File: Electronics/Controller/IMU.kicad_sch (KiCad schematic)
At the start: 9 parts, among them J10 CAN BUS, J9 TERM, U5 TJA1462ATK-0Z, U6 PESD2CANFD24V-TR

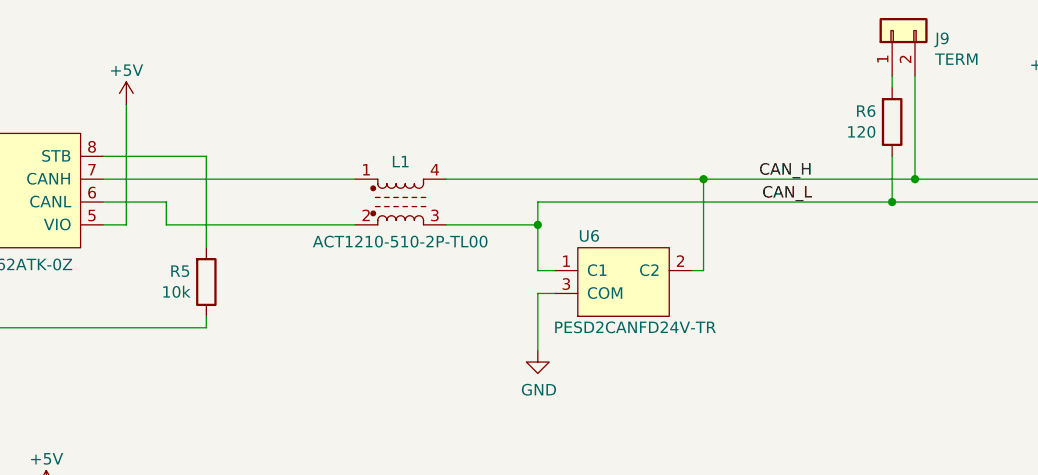
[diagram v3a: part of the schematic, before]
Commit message: Changed switches and lamps. Removed status LEDs. Working on PCB layout.
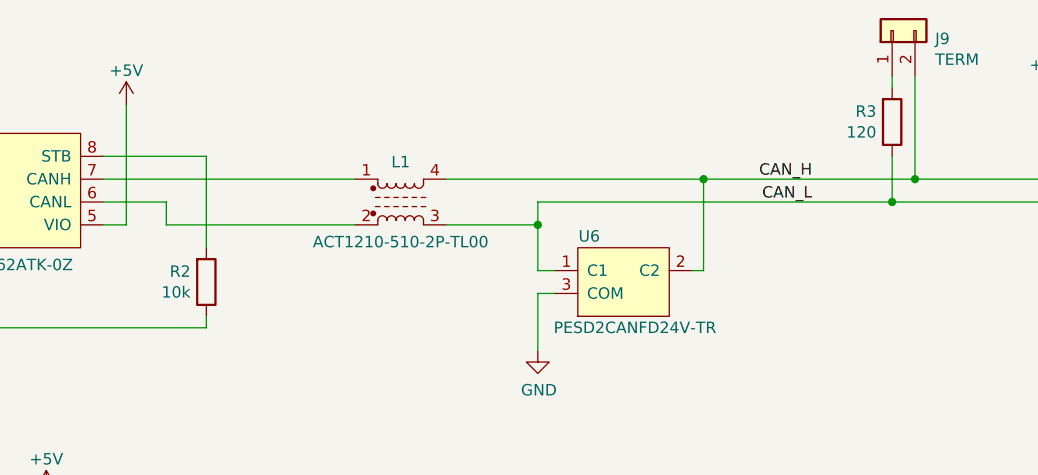
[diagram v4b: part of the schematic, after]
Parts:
- renumbered R5 to R2, R6 to R3
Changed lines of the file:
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@@
   (title_block
     (title "Tandem Leveller Controller")
-    (date "2025-02-16")
+    (date "2025-02-18")
     (rev "V1.0")
     (company "(C) andy@britishideas.com 2025")
@@
   (symbol (lib_id "power:GND") (at 215.265 92.71 0) (unit 1)
     (in_bom yes) (on_board yes) (dnp no)
-    (property "Reference" "#PWR026" (at 215.265 99.06 0)
+    (property "Reference" "#PWR023" (at 215.265 99.06 0)
       (effects (font (size 1.27 1.27)) hide)
     )
@@
       (project "Tandem Leveller Controller"
         (path "/56ffd1a6-bbed-43b6-8aa8-f23f49f76448/acdcb949-8386-481e-9890-88fc97609208"
-          (reference "#PWR026") (unit 1)
+          (reference "#PWR023") (unit 1)
         )
       )
@@
   (symbol (lib_id "power:+5V") (at 96.52 119.38 0) (unit 1)
     (in_bom yes) (on_board yes) (dnp no)
-    (property "Reference" "#PWR021" (at 96.52 123.19 0)
+    (property "Reference" "#PWR018" (at 96.52 123.19 0)
       (effects (font (size 1.27 1.27)) hide)
     )
@@
       (project "Tandem Leveller Controller"
         (path "/56ffd1a6-bbed-43b6-8aa8-f23f49f76448/acdcb949-8386-481e-9890-88fc97609208"
-          (reference "#PWR021") (unit 1)
+          (reference "#PWR018") (unit 1)
         )
       )
@@
   (symbol (lib_id "power:+5V") (at 85.725 119.38 0) (unit 1)
     (in_bom yes) (on_board yes) (dnp no)
-    (property "Reference" "#PWR019" (at 85.725 123.19 0)
+    (property "Reference" "#PWR016" (at 85.725 123.19 0)
       (effects (font (size 1.27 1.27)) hide)
     )
@@
       (project "Tandem Leveller Controller"
         (path "/56ffd1a6-bbed-43b6-8aa8-f23f49f76448/acdcb949-8386-481e-9890-88fc97609208"
-          (reference "#PWR019") (unit 1)
+          (reference "#PWR016") (unit 1)
         )
       )
@@
   (symbol (lib_id "Device:R") (at 190.5 78.105 0) (mirror x) (unit 1)
     (in_bom yes) (on_board yes) (dnp no)
-    (property "Reference" "R6" (at 188.7474 76.9366 0)
+    (property "Reference" "R3" (at 188.7474 76.9366 0)
       (effects (font (size 1.27 1.27)) (justify right))
     )
@@
       (project "Tandem Leveller Controller"
         (path "/56ffd1a6-bbed-43b6-8aa8-f23f49f76448/acdcb949-8386-481e-9890-88fc97609208"
-          (reference "R6") (unit 1)
+          (reference "R3") (unit 1)
         )
       )
@@
   (symbol (lib_id "power:GND") (at 79.375 102.235 0) (unit 1)
     (in_bom yes) (on_board yes) (dnp no)
-    (property "Reference" "#PWR018" (at 79.375 108.585 0)
+    (property "Reference" "#PWR015" (at 79.375 108.585 0)
       (effects (font (size 1.27 1.27)) hide)
     )
@@
       (project "Tandem Leveller Controller"
         (path "/56ffd1a6-bbed-43b6-8aa8-f23f49f76448/acdcb949-8386-481e-9890-88fc97609208"
-          (reference "#PWR018") (unit 1)
+          (reference "#PWR015") (unit 1)
         )
       )
@@
   (symbol (lib_id "power:+5V") (at 207.645 75.565 0) (unit 1)
     (in_bom yes) (on_board yes) (dnp no)
-    (property "Reference" "#PWR024" (at 207.645 79.375 0)
+    (property "Reference" "#PWR021" (at 207.645 79.375 0)
       (effects (font (size 1.27 1.27)) hide)
     )
@@
       (project "Tandem Leveller Controller"
         (path "/56ffd1a6-bbed-43b6-8aa8-f23f49f76448/acdcb949-8386-481e-9890-88fc97609208"
-          (reference "#PWR024") (unit 1)
+          (reference "#PWR021") (unit 1)
         )
       )
@@
   (symbol (lib_id "power:+5V") (at 105.41 76.2 0) (unit 1)
     (in_bom yes) (on_board yes) (dnp no)
-    (property "Reference" "#PWR022" (at 105.41 80.01 0)
+    (property "Reference" "#PWR019" (at 105.41 80.01 0)
       (effects (font (size 1.27 1.27)) hide)
     )
@@
       (project "Tandem Leveller Controller"
         (path "/56ffd1a6-bbed-43b6-8aa8-f23f49f76448/acdcb949-8386-481e-9890-88fc97609208"
-          (reference "#PWR022") (unit 1)
+          (reference "#PWR019") (unit 1)
         )
       )
@@
   (symbol (lib_id "power:GND") (at 151.13 103.505 0) (unit 1)
     (in_bom yes) (on_board yes) (dnp no)
-    (property "Reference" "#PWR023" (at 151.13 109.855 0)
+    (property "Reference" "#PWR020" (at 151.13 109.855 0)
       (effects (font (size 1.27 1.27)) hide)
     )
@@
       (project "Tandem Leveller Controller"
         (path "/56ffd1a6-bbed-43b6-8aa8-f23f49f76448/acdcb949-8386-481e-9890-88fc97609208"
-          (reference "#PWR023") (unit 1)
+          (reference "#PWR020") (unit 1)
         )
       )
@@
   (symbol (lib_id "Device:R") (at 114.3 95.885 0) (mirror x) (unit 1)
     (in_bom yes) (on_board yes) (dnp no)
-    (property "Reference" "R5" (at 112.5474 94.7166 0)
+    (property "Reference" "R2" (at 112.5474 94.7166 0)
       (effects (font (size 1.27 1.27)) (justify right))
     )
@@
       (project "Tandem Leveller Controller"
         (path "/56ffd1a6-bbed-43b6-8aa8-f23f49f76448/acdcb949-8386-481e-9890-88fc97609208"
-          (reference "R5") (unit 1)
+          (reference "R2") (unit 1)
         )
       )
@@
   (symbol (lib_id "power:+5V") (at 78.105 76.2 0) (unit 1)
     (in_bom yes) (on_board yes) (dnp no)
-    (property "Reference" "#PWR017" (at 78.105 80.01 0)
+    (property "Reference" "#PWR014" (at 78.105 80.01 0)
       (effects (font (size 1.27 1.27)) hide)
     )
@@
       (project "Tandem Leveller Controller"
         (path "/56ffd1a6-bbed-43b6-8aa8-f23f49f76448/acdcb949-8386-481e-9890-88fc97609208"
+          (reference "#PWR014") (unit 1)
+        )
+      )
+    )
+  )
+  (symbol (lib_id "power:GND") (at 85.725 133.985 0) (unit 1)
+    (in_bom yes) (on_board yes) (dnp no)
+    (property "Reference" "#PWR017" (at 85.725 140.335 0)
+      (effects (font (size 1.27 1.27)) hide)
+    )
+    (property "Value" "GND" (at 85.852 138.3792 0)
+      (effects (font (size 1.27 1.27)))
+    )
+    (property "Footprint" "" (at 85.725 133.985 0)
+      (effects (font (size 1.27 1.27)) hide)
+    )
+    (property "Datasheet" "" (at 85.725 133.985 0)
+      (effects (font (size 1.27 1.27)) hide)
+    )
+    (pin "1")
+    (instances
+      (project "Tandem Leveller Controller"
+        (path "/56ffd1a6-bbed-43b6-8aa8-f23f49f76448/acdcb949-8386-481e-9890-88fc97609208"
           (reference "#PWR017") (unit 1)
         )
@@
     )
   )
-  (symbol (lib_id "power:GND") (at 85.725 133.985 0) (unit 1)
-    (in_bom yes) (on_board yes) (dnp no)
-    (property "Reference" "#PWR020" (at 85.725 140.335 0)
-      (effects (font (size 1.27 1.27)) hide)
-    )
-    (property "Value" "GND" (at 85.852 138.3792 0)
-      (effects (font (size 1.27 1.27)))
-    )
-    (property "Footprint" "" (at 85.725 133.985 0)
-      (effects (font (size 1.27 1.27)) hide)
-    )
-    (property "Datasheet" "" (at 85.725 133.985 0)
-      (effects (font (size 1.27 1.27)) hide)
-    )
-    (pin "1")
-    (instances
-      (project "Tandem Leveller Controller"
-        (path "/56ffd1a6-bbed-43b6-8aa8-f23f49f76448/acdcb949-8386-481e-9890-88fc97609208"
-          (reference "#PWR020") (unit 1)
-        )
-      )
-    )
-  )
   (symbol (lib_id "EmSA:PESD2CANFD24V-T") (at 155.575 99.695 0) (unit 1)
     (in_bom yes) (on_board yes) (dnp no)
@@
   (symbol (lib_id "power:+12V") (at 215.265 75.565 0) (unit 1)
     (in_bom yes) (on_board yes) (dnp no)
-    (property "Reference" "#PWR025" (at 215.265 79.375 0)
+    (property "Reference" "#PWR022" (at 215.265 79.375 0)
       (effects (font (size 1.27 1.27)) hide)
     )
@@
       (project "Tandem Leveller Controller"
         (path "/56ffd1a6-bbed-43b6-8aa8-f23f49f76448/acdcb949-8386-481e-9890-88fc97609208"
-          (reference "#PWR025") (unit 1)
-        )
-      )
+          (reference "#PWR022") (unit 1)
+        )
+      )

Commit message: Working on PCB layout.
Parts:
- added J23: CAN, EmSA:DB9_RA_MALE_LD09P13A4, symbol Connector:DB9_Male
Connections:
- net CAN_H: now also J23.7
- net CAN_L: now also J23.2
- net GND: now also J23.3, J23.6
- no-connect marks 0 -> 5
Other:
- moved on the sheet: C1, C2, J10, J9, L1, R2, R3, U5, U6

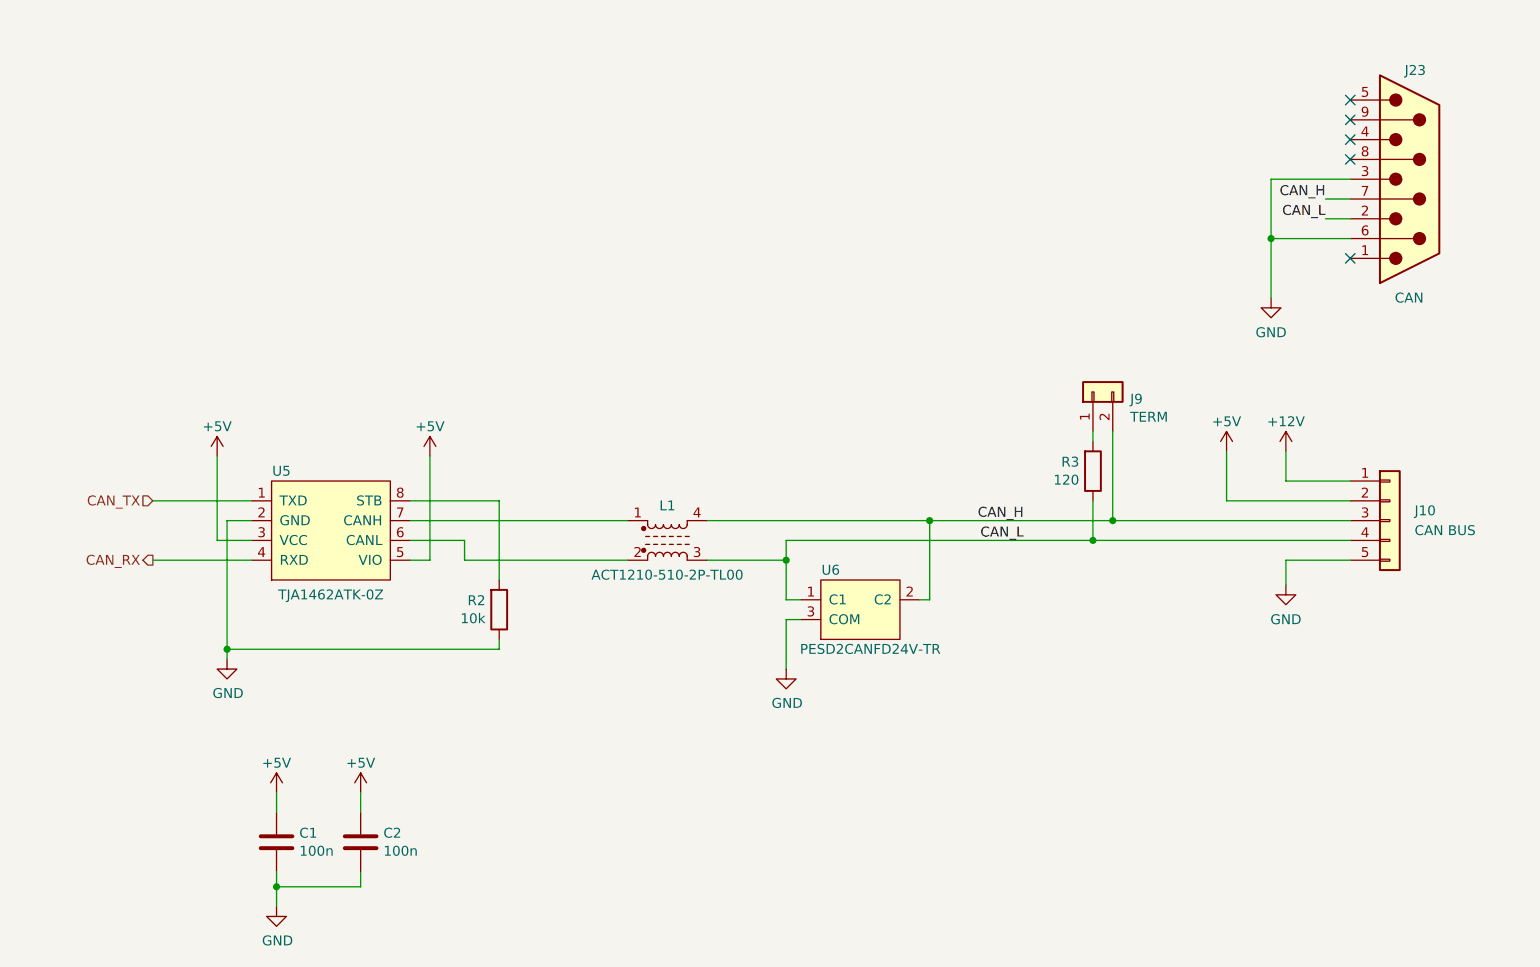
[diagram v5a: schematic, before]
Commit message: Moved controls from GPIO to CAN bus. Added two more CAN bus connectors. Changed GNSS SIM connector from pin header to JST-PH.
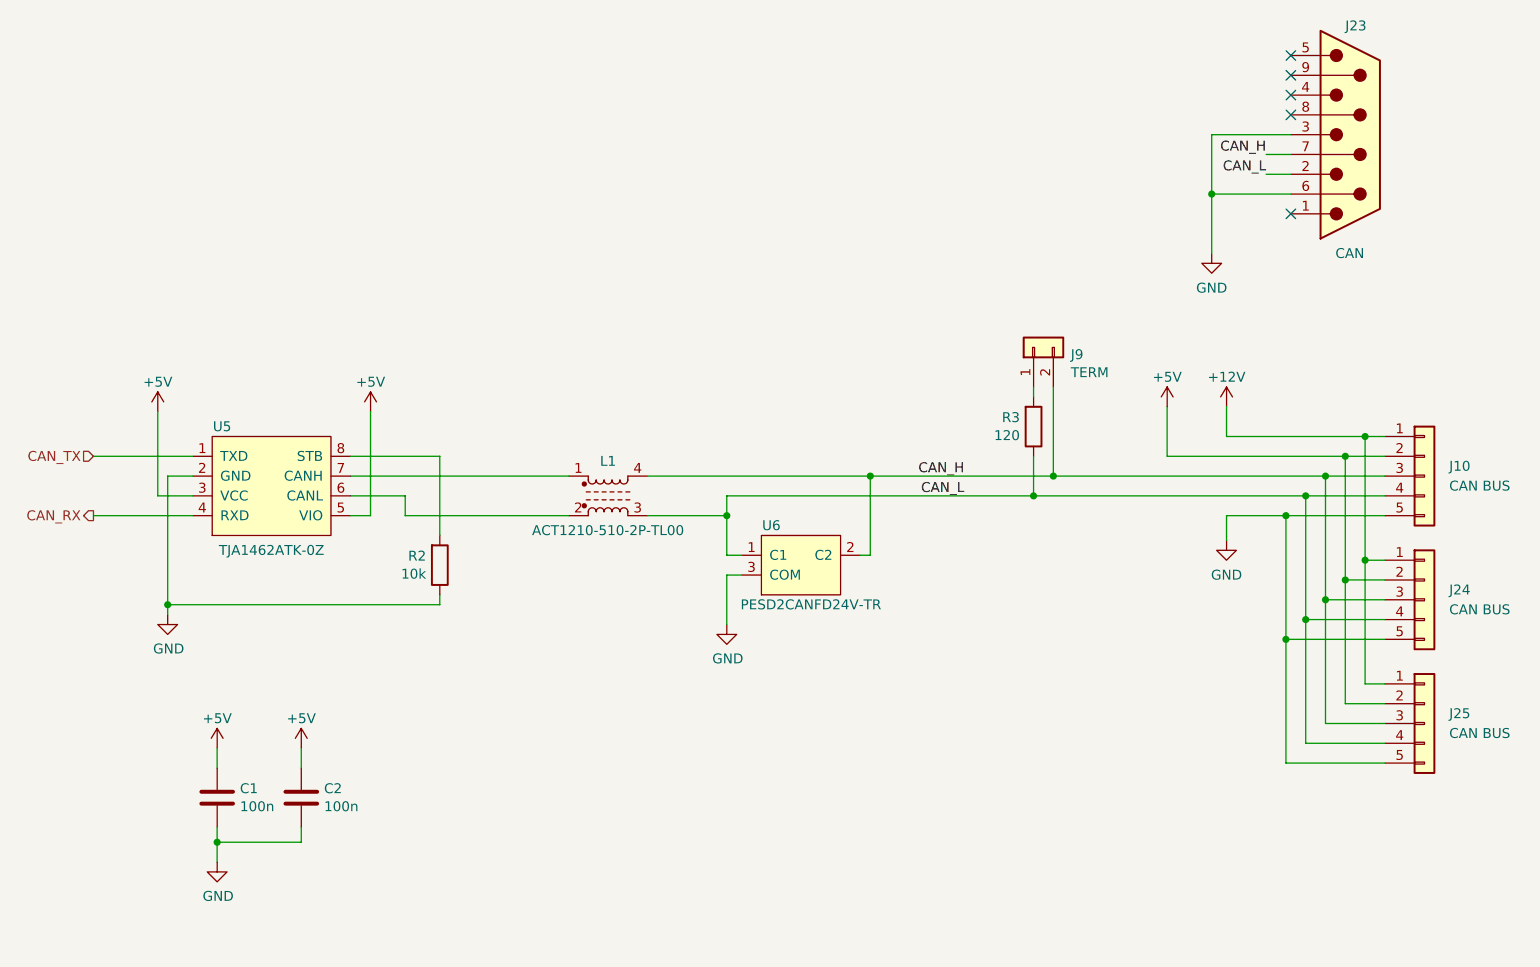
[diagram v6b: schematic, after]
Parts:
- added J24, J25: CAN BUS, Connector_JST:JST_PH_B5B-PH-K_1x05_P2.00mm_Vertical, symbol Connector_Generic:Conn_01x05
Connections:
- net +12V: now also J24.1 (Pin_1), J25.1 (Pin_1)
- net +5V: now also J24.2 (Pin_2), J25.2 (Pin_2)
- net CAN_H: now also J24.3 (Pin_3), J25.3 (Pin_3)
- net CAN_L: now also J24.4 (Pin_4), J25.4 (Pin_4)
- net GND: now also J24.5 (Pin_5), J25.5 (Pin_5)
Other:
- moved on the sheet: C1, C2, J10, J23, J9, L1, R2, R3, U5, U6

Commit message: Added 4.7uF caps to FT232RL on controller.
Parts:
- C1, C2: LCSC (none) -> C1711
- J10, J24, J25: LCSC (none) -> C157993
- J23: LCSC (none) -> C3103673
- J9: LCSC (none) -> C7494857
- L1: LCSC (none) -> C95572
- R2: LCSC (none) -> C17414
- R3: LCSC (none) -> C17437
- U5: LCSC (none) -> C3229259
- U6: LCSC (none) -> C552486
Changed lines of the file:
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@@
   (title_block
     (title "Tandem Leveller Controller")
-    (date "2025-02-22")
+    (date "2025-03-11")
     (rev "V1.0")
     (company "(C) andy@britishideas.com 2025")
@@
       (effects (font (size 1.27 1.27)) hide)
     )
+    (property "LCSC" "C157993" (at 229.235 96.52 0)
+      (effects (font (size 1.27 1.27)) hide)
+    )
     (pin "2")
     (pin "5")
@@
       (effects (font (size 1.27 1.27)) hide)
     )
+    (property "LCSC" "C157993" (at 229.235 112.395 0)
+      (effects (font (size 1.27 1.27)) hide)
+    )
     (pin "2")
     (pin "5")
@@
       (effects (font (size 1.27 1.27)) hide)
     )
+    (property "LCSC" "C157993" (at 229.235 128.27 0)
+      (effects (font (size 1.27 1.27)) hide)
+    )
     (pin "2")
     (pin "5")
@@
       (effects (font (size 1.27 1.27)) hide)
     )
+    (property "LCSC" "C1711" (at 74.295 137.795 0)
+      (effects (font (size 1.27 1.27)) hide)
+    )
     (pin "1")
     (pin "2")
@@
       (effects (font (size 1.27 1.27)) hide)
     )
+    (property "LCSC" "C17437" (at 179.07 90.17 0)
+      (effects (font (size 1.27 1.27)) hide)
+    )
     (pin "1")
     (pin "2")
@@
     )
     (property "manf#" "ACT1210-510-2P-TL00" (at 124.46 99.06 0)
+      (effects (font (size 1.27 1.27)) hide)
+    )
+    (property "LCSC" "C95572" (at 124.46 99.06 0)
       (effects (font (size 1.27 1.27)) hide)
     )
@@
       (effects (font (size 1.27 1.27)) hide)
     )
+    (property "LCSC" "C7494857" (at 179.07 80.01 0)
+      (effects (font (size 1.27 1.27)) hide)
+    )
     (pin "1")
     (pin "2")
@@
       (effects (font (size 1.27 1.27)) hide)
     )
+    (property "LCSC" "C1711" (at 85.09 137.795 0)
+      (effects (font (size 1.27 1.27)) hide)
+    )
     (pin "1")
     (pin "2")
@@
     )
     (property "manf#" "L717SDEH09PVF" (at 219.71 52.705 0)
+      (effects (font (size 1.27 1.27)) hide)
+    )
+    (property "LCSC" "C3103673" (at 219.71 52.705 0)
       (effects (font (size 1.27 1.27)) hide)
     )
@@
       (effects (font (size 1.27 1.27)) hide)
     )
+    (property "LCSC" "C3229259" (at 73.66 104.14 0)
+      (effects (font (size 1.27 1.27)) hide)
+    )
     (pin "1")
     (pin "2")
@@
       (effects (font (size 1.27 1.27)) hide)
     )
+    (property "LCSC" "C17414" (at 102.87 107.95 0)
+      (effects (font (size 1.27 1.27)) hide)
+    )
     (pin "1")
     (pin "2")
@@
       (effects (font (size 1.27 1.27)) hide)
     )
+    (property "LCSC" "C552486" (at 144.145 111.76 0)
+      (effects (font (size 1.27 1.27)) hide)
+    )
